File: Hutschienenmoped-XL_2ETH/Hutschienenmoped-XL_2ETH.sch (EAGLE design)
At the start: 118 parts, among them J1 638207222005, J13 638207222005, J15 638207222008, J2 645004114822, J3 61302211821, J4 61300421121, J6 61302211821, J7 638207222005, J8 638207222007, U1 ESP32-S3-DEVKITC-1-N8R2, U4 TLE9250VSJ

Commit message: gitflow-feature-stash: ETH
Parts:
- removed J3, J6: 61302211821, Wurth_Connectors_WR-PHD:6130XX11821_61302211821
- added ESP32-J1, ESP32-J3: 61302211821, Wurth_Connectors_WR-PHD:6130XX11821_61302211821
- added J10: 61300811821, Wurth_Connectors_WR-PHD:6130XX11821_61300811821
- added J11: 61300611821, Wurth_Connectors_WR-PHD:6130XX11821_61300611821
- added J12: 61300615721, Wurth_Connectors_WR-PHD:6130XX15721_61300615721
- added J14: 61300815721, Wurth_Connectors_WR-PHD:6130XX15721_61300815721
- added MP1, MP2, MP3, MP4: M3 x 2.5mm, Wurth_Assembly_WA-SMSI:WA-SMSI_9774XXX360_9774025360R
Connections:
- removed net IX00: U1.GPIO14
- removed net IX06: U1.GPIO15
- removed net MB_UART_RTS1: U1.GPIO10
- removed net MB_UART_RXD1: U1.GPIO8
- removed net MB_UART_RXD2: U1.GPIO11
- removed net QX06: U1.GPIO48
- removed net QX07: U1.GPIO38
- net +3V3: now also ESP32-J1.1, ESP32-J1.2
- net +5V: now also ESP32-J1.21
- net BOOT: now also ESP32-J3.14
- net CAN1_RXD: now also ESP32-J1.5
- net CAN1_TXD: now also ESP32-J1.4
- net CI1: now also ESP32-J1.19
- net CI2: now also ESP32-J1.18
- net CI3: now also ESP32-J1.15
- net CI4: now also ESP32-J1.13
- net CI5: now also ESP32-J1.11
- net CI6: now also ESP32-J1.10
- net CI7: now also ESP32-J1.7
- net CI8: now also ESP32-J1.6
- net ECU_GND: now also ESP32-J1.22, ESP32-J3.1, ESP32-J3.21, ESP32-J3.22
- net Q1C: now also ESP32-J3.18
- net Q2C: now also ESP32-J3.17
- net Q3C: now also ESP32-J3.9
- net Q4C: now also ESP32-J3.8
- net Q5C: now also ESP32-J3.7
- net Q6C: now also ESP32-J3.6
- net Q7C: now also ESP32-J3.4
- net Q8C: now also ESP32-J3.5
- net RESET: now also ESP32-J1.3

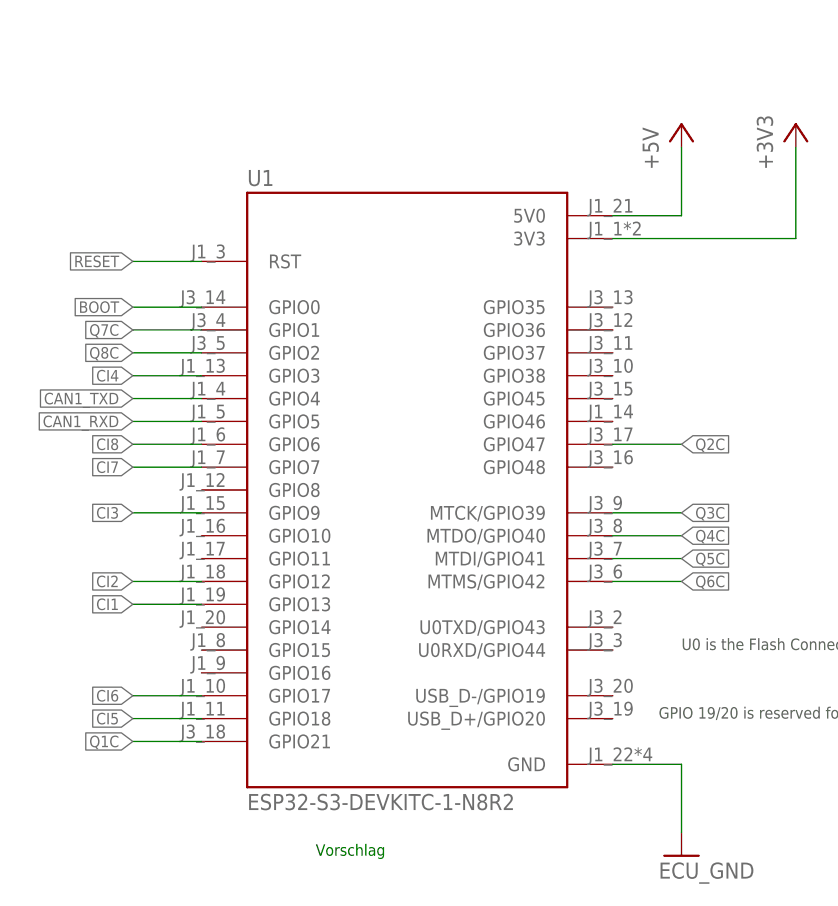
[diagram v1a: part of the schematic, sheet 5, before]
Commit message: Add new wire connections and curves in the board design.
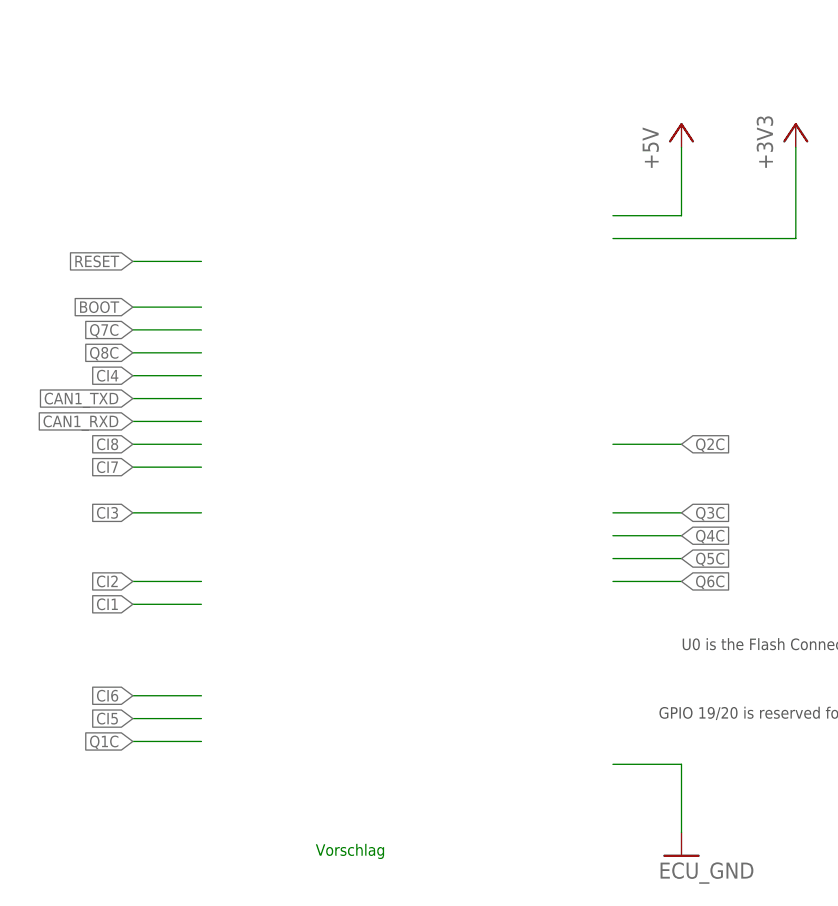
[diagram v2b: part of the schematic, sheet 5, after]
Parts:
- removed U1: ESP32-S3-DEVKITC-1-N8R2, ESP32-S3-DEVKITC-1-N8R2:ESP32-S3-DEVKITC-1-N8R2
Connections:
- net +3V3: no longer U1.3V3
- net +5V: no longer U1.5V0
- net BOOT: no longer U1.GPIO0
- net CAN1_RXD: no longer U1.GPIO5
- net CAN1_TXD: no longer U1.GPIO4
- net CI1: no longer U1.GPIO13
- net CI2: no longer U1.GPIO12
- net CI3: no longer U1.GPIO9
- net CI4: no longer U1.GPIO3
- net CI5: no longer U1.GPIO18
- net CI6: no longer U1.GPIO17
- net CI7: no longer U1.GPIO7
- net CI8: no longer U1.GPIO6
- net ECU_GND: no longer U1.GND
- net Q1C: no longer U1.GPIO21
- net Q2C: no longer U1.GPIO47
- net Q3C: no longer U1.MTCK/GPIO39
- net Q4C: no longer U1.MTDO/GPIO40
- net Q5C: no longer U1.MTDI/GPIO41
- net Q6C: no longer U1.MTMS/GPIO42
- net Q7C: no longer U1.GPIO1
- net Q8C: no longer U1.GPIO2
- net RESET: no longer U1.RST
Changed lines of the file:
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@@
 <part name="D3" library="Wurth_LEDs_WL-SMTW" library_urn="urn:adsk.eagle:library:19062651" deviceset="WL-SMTW_3528" device="" package3d_urn="urn:adsk.eagle:package:19062500/6" technology="_150141VS73100" value="150141VS73100"/>
 <part name="FRAME3" library="frames" library_urn="urn:adsk.eagle:library:229" deviceset="A4L-LOC" device=""/>
-<part name="U1" library="ESP32-S3-DEVKITC-1-N8R2" library_urn="urn:adsk.eagle:library:34329045" deviceset="ESP32-S3-DEVKITC-1-N8R2" device="" package3d_urn="urn:adsk.eagle:package:34329048/2"/>
 <part name="+3V4" library="supply1" library_urn="urn:adsk.eagle:library:371" deviceset="+3V3" device=""/>
 <part name="P+5" library="supply1" library_urn="urn:adsk.eagle:library:371" deviceset="+5V" device=""/>
@@
 <attribute name="SHEET" x="230.505" y="5.08" size="2.54" layer="94" font="vector"/>
 </instance>
-<instance part="U1" gate="G$1" x="111.76" y="83.82" smashed="yes">
-<attribute name="NAME" x="93.98" y="119.38" size="1.778" layer="95" align="top-left"/>
-<attribute name="VALUE" x="93.98" y="48.26" size="1.778" layer="96"/>
-</instance>
 <instance part="+3V4" gate="G$1" x="154.94" y="124.46" smashed="yes">
 <attribute name="VALUE" x="152.4" y="119.38" size="1.778" layer="96" rot="R90"/>
@@
 <net name="+3V3" class="0">
 <segment>
-<pinref part="U1" gate="G$1" pin="3V3"/>
 <pinref part="+3V4" gate="G$1" pin="+3V3"/>
 <wire x1="134.62" y1="111.76" x2="154.94" y2="111.76" width="0.1524" layer="91"/>
@@
 <net name="CAN1_TXD" class="0">
 <segment>
-<pinref part="U1" gate="G$1" pin="GPIO4"/>
 <wire x1="88.9" y1="93.98" x2="81.28" y2="93.98" width="0.1524" layer="91"/>
 <label x="81.28" y="93.98" size="1.27" layer="95" rot="R180" xref="yes"/>
@@
 <net name="CAN1_RXD" class="0">
 <segment>
-<pinref part="U1" gate="G$1" pin="GPIO5"/>
 <wire x1="88.9" y1="91.44" x2="81.28" y2="91.44" width="0.1524" layer="91"/>
 <label x="81.28" y="91.44" size="1.27" layer="95" rot="R180" xref="yes"/>
@@
 <net name="CI7" class="0">
 <segment>
-<pinref part="U1" gate="G$1" pin="GPIO7"/>
 <wire x1="88.9" y1="86.36" x2="81.28" y2="86.36" width="0.1524" layer="91"/>
 <label x="81.28" y="86.36" size="1.27" layer="95" rot="R180" xref="yes"/>
@@
 <net name="CI5" class="0">
 <segment>
-<pinref part="U1" gate="G$1" pin="GPIO18"/>
 <wire x1="88.9" y1="58.42" x2="81.28" y2="58.42" width="0.1524" layer="91"/>
 <label x="81.28" y="58.42" size="1.27" layer="95" rot="R180" xref="yes"/>
@@
 <net name="CI8" class="0">
 <segment>
-<pinref part="U1" gate="G$1" pin="GPIO6"/>
 <wire x1="88.9" y1="88.9" x2="81.28" y2="88.9" width="0.1524" layer="91"/>
 <label x="81.28" y="88.9" size="1.27" layer="95" rot="R180" xref="yes"/>
@@
 <net name="Q1C" class="0">
 <segment>
-<pinref part="U1" gate="G$1" pin="GPIO21"/>
 <wire x1="88.9" y1="55.88" x2="81.28" y2="55.88" width="0.1524" layer="91"/>
 <label x="81.28" y="55.88" size="1.27" layer="95" rot="R180" xref="yes"/>
@@
 <net name="Q3C" class="0">
 <segment>
-<pinref part="U1" gate="G$1" pin="MTCK/GPIO39"/>
 <wire x1="134.62" y1="81.28" x2="142.24" y2="81.28" width="0.1524" layer="91"/>
 <label x="142.24" y="81.28" size="1.27" layer="95" xref="yes"/>
@@
 <net name="BOOT" class="0">
 <segment>
-<pinref part="U1" gate="G$1" pin="GPIO0"/>
 <wire x1="88.9" y1="104.14" x2="81.28" y2="104.14" width="0.1524" layer="91"/>
 <label x="81.28" y="104.14" size="1.27" layer="95" rot="R180" xref="yes"/>
@@
 <net name="RESET" class="0">
 <segment>
-<pinref part="U1" gate="G$1" pin="RST"/>
 <wire x1="88.9" y1="109.22" x2="81.28" y2="109.22" width="0.1524" layer="91"/>
 <label x="81.28" y="109.22" size="1.27" layer="95" rot="R180" xref="yes"/>
@@
 <net name="CI4" class="0">
 <segment>
-<pinref part="U1" gate="G$1" pin="GPIO3"/>
 <wire x1="88.9" y1="96.52" x2="81.28" y2="96.52" width="0.1524" layer="91"/>
 <label x="81.28" y="96.52" size="1.27" layer="95" rot="R180" xref="yes"/>
@@
 <net name="CI6" class="0">
 <segment>
-<pinref part="U1" gate="G$1" pin="GPIO17"/>
 <wire x1="88.9" y1="60.96" x2="81.28" y2="60.96" width="0.1524" layer="91"/>
 <label x="81.28" y="60.96" size="1.27" layer="95" rot="R180" xref="yes"/>
@@
 <net name="Q5C" class="0">
 <segment>
-<pinref part="U1" gate="G$1" pin="MTDI/GPIO41"/>
 <wire x1="134.62" y1="76.2" x2="142.24" y2="76.2" width="0.1524" layer="91"/>
 <label x="142.24" y="76.2" size="1.27" layer="95" xref="yes"/>
@@
 <net name="Q4C" class="0">
 <segment>
-<pinref part="U1" gate="G$1" pin="MTDO/GPIO40"/>
 <wire x1="134.62" y1="78.74" x2="142.24" y2="78.74" width="0.1524" layer="91"/>
 <label x="142.24" y="78.74" size="1.27" layer="95" xref="yes"/>
@@
 <net name="Q6C" class="0">
 <segment>
-<pinref part="U1" gate="G$1" pin="MTMS/GPIO42"/>
 <wire x1="134.62" y1="73.66" x2="142.24" y2="73.66" width="0.1524" layer="91"/>
 <label x="142.24" y="73.66" size="1.27" layer="95" xref="yes"/>
@@
 <net name="Q8C" class="0">
 <segment>
-<pinref part="U1" gate="G$1" pin="GPIO2"/>
 <wire x1="88.9" y1="99.06" x2="81.28" y2="99.06" width="0.1524" layer="91"/>
 <label x="81.28" y="99.06" size="1.27" layer="95" rot="R180" xref="yes"/>
@@
 <net name="Q2C" class="0">
 <segment>
-<pinref part="U1" gate="G$1" pin="GPIO47"/>
 <wire x1="134.62" y1="88.9" x2="142.24" y2="88.9" width="0.1524" layer="91"/>
 <label x="142.24" y="88.9" size="1.27" layer="95" xref="yes"/>
@@
 <net name="CI3" class="0">
 <segment>
-<pinref part="U1" gate="G$1" pin="GPIO9"/>
 <wire x1="88.9" y1="81.28" x2="81.28" y2="81.28" width="0.1524" layer="91"/>
 <label x="81.28" y="81.28" size="1.27" layer="95" rot="R180" xref="yes"/>
@@
 <net name="CI2" class="0">
 <segment>
-<pinref part="U1" gate="G$1" pin="GPIO12"/>
 <wire x1="88.9" y1="73.66" x2="81.28" y2="73.66" width="0.1524" layer="91"/>
 <label x="81.28" y="73.66" size="1.27" layer="95" rot="R180" xref="yes"/>
@@
 <net name="CI1" class="0">
 <segment>
-<pinref part="U1" gate="G$1" pin="GPIO13"/>
 <wire x1="88.9" y1="71.12" x2="81.28" y2="71.12" width="0.1524" layer="91"/>
 <label x="81.28" y="71.12" size="1.27" layer="95" rot="R180" xref="yes"/>
@@
 <net name="Q7C" class="0">
 <segment>
-<pinref part="U1" gate="G$1" pin="GPIO1"/>
 <wire x1="88.9" y1="101.6" x2="81.28" y2="101.6" width="0.1524" layer="91"/>
 <label x="81.28" y="101.6" size="1.27" layer="95" rot="R180" xref="yes"/>
@@
 <net name="ECU_GND" class="1">
 <segment>
-<pinref part="U1" gate="G$1" pin="GND"/>
 <wire x1="134.62" y1="53.34" x2="142.24" y2="53.34" width="0.1524" layer="91"/>
 <wire x1="142.24" y1="53.34" x2="142.24" y2="45.72" width="0.1524" layer="91"/>
@@
 <net name="+5V" class="0">
 <segment>
-<pinref part="U1" gate="G$1" pin="5V0"/>
 <pinref part="P+5" gate="1" pin="+5V"/>
 <wire x1="134.62" y1="114.3" x2="142.24" y2="114.3" width="0.1524" layer="91"/>

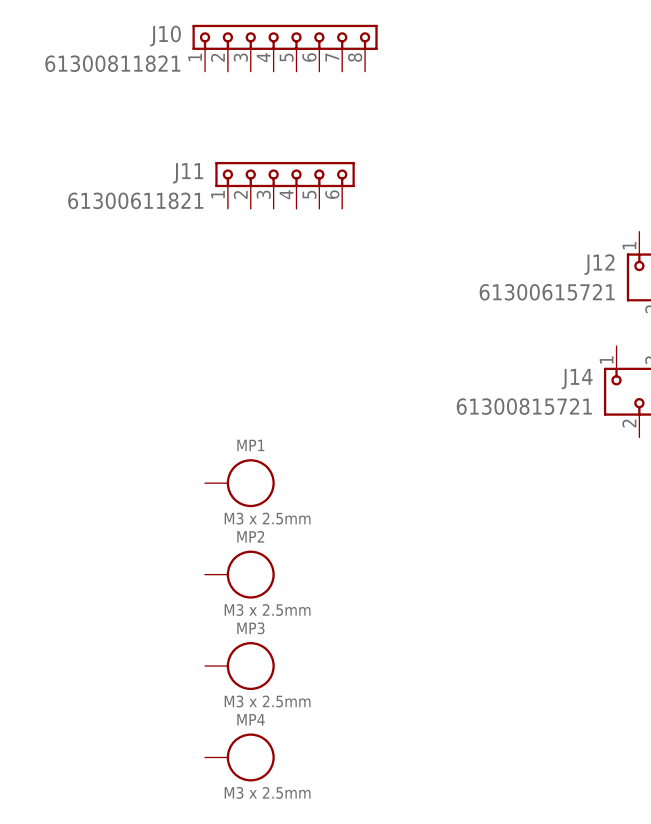
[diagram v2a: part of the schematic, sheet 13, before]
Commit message: Update grid settings to display grid lines, add wires for a new component. Remove redundant package elements and attributes.
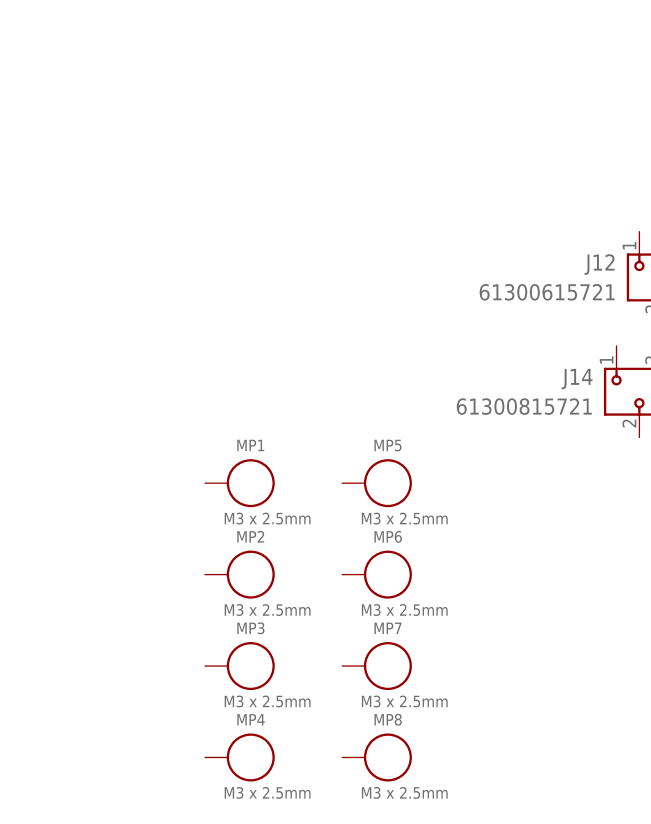
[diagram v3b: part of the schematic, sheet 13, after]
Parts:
- removed J10: 61300811821, Wurth_Connectors_WR-PHD:6130XX11821_61300811821
- removed J11: 61300611821, Wurth_Connectors_WR-PHD:6130XX11821_61300611821
- added MP5, MP6, MP7, MP8: M3 x 2.5mm, Wurth_Assembly_WA-SMSI:WA-SMSI_9774XXX360_9774025360R
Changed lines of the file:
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@@
 <part name="J1" library="Wurth_Connectors_WR-FAST" library_urn="urn:adsk.eagle:library:15267884" deviceset="638207222005" device="" package3d_urn="urn:adsk.eagle:package:15267960/3" value=" 638207222005 "/>
 <part name="J2" library="Wurth_Connectors_WR-WTB" library_urn="urn:adsk.eagle:library:15818693" deviceset="645004114822" device="" package3d_urn="urn:adsk.eagle:package:15819025/2" value="645004114822"/>
-<part name="J10" library="Wurth_Connectors_WR-PHD" library_urn="urn:adsk.eagle:library:14804658" deviceset="6130XX11821_61300811821" device="" package3d_urn="urn:adsk.eagle:package:14805545/3" value=" 61300811821 "/>
-<part name="J11" library="Wurth_Connectors_WR-PHD" library_urn="urn:adsk.eagle:library:14804658" deviceset="6130XX11821_61300611821" device="" package3d_urn="urn:adsk.eagle:package:14805543/3" value=" 61300611821 "/>
 <part name="MP1" library="Wurth_Assembly_WA-SMSI" library_urn="urn:adsk.eagle:library:14418591" deviceset="WA-SMSI_9774XXX360" device="_9774025360R" package3d_urn="urn:adsk.eagle:package:14321862/4" value="M3 x 2.5mm"/>
 <part name="MP2" library="Wurth_Assembly_WA-SMSI" library_urn="urn:adsk.eagle:library:14418591" deviceset="WA-SMSI_9774XXX360" device="_9774025360R" package3d_urn="urn:adsk.eagle:package:14321862/4" value="M3 x 2.5mm"/>
@@
 <part name="FRAME1" library="frames" library_urn="urn:adsk.eagle:library:229" deviceset="A4L-LOC" device=""/>
 <part name="P+1" library="supply1" library_urn="urn:adsk.eagle:library:371" deviceset="+5V" device=""/>
+<part name="MP5" library="Wurth_Assembly_WA-SMSI" library_urn="urn:adsk.eagle:library:14418591" deviceset="WA-SMSI_9774XXX360" device="_9774025360R" package3d_urn="urn:adsk.eagle:package:14321862/4" value="M3 x 2.5mm"/>
+<part name="MP6" library="Wurth_Assembly_WA-SMSI" library_urn="urn:adsk.eagle:library:14418591" deviceset="WA-SMSI_9774XXX360" device="_9774025360R" package3d_urn="urn:adsk.eagle:package:14321862/4" value="M3 x 2.5mm"/>
+<part name="MP7" library="Wurth_Assembly_WA-SMSI" library_urn="urn:adsk.eagle:library:14418591" deviceset="WA-SMSI_9774XXX360" device="_9774025360R" package3d_urn="urn:adsk.eagle:package:14321862/4" value="M3 x 2.5mm"/>
+<part name="MP8" library="Wurth_Assembly_WA-SMSI" library_urn="urn:adsk.eagle:library:14418591" deviceset="WA-SMSI_9774XXX360" device="_9774025360R" package3d_urn="urn:adsk.eagle:package:14321862/4" value="M3 x 2.5mm"/>
 </parts>
 <sheets>
@@
 </plain>
 <instances>
-<instance part="J10" gate="G$1" x="68.58" y="170.18" smashed="yes">
-<attribute name="NAME" x="58.42" y="168.402" size="1.778" layer="95" align="bottom-right"/>
-<attribute name="VALUE" x="58.42" y="165.1" size="1.778" layer="96" align="bottom-right"/>
-</instance>
-<instance part="J11" gate="G$1" x="71.12" y="154.94" smashed="yes">
-<attribute name="NAME" x="60.96" y="153.162" size="1.778" layer="95" align="bottom-right"/>
-<attribute name="VALUE" x="60.96" y="149.86" size="1.778" layer="96" align="bottom-right"/>
-</instance>
 <instance part="MP1" gate="G$1" x="66.04" y="119.38" smashed="yes">
 <attribute name="NAME" x="66.04" y="122.936" size="1.27" layer="95" align="bottom-center"/>
@@
 <attribute name="VALUE" x="104.14" y="127" size="1.778" layer="96" align="bottom-right"/>
 </instance>
+<instance part="MP5" gate="G$1" x="81.28" y="119.38" smashed="yes">
+<attribute name="NAME" x="81.28" y="122.936" size="1.27" layer="95" align="bottom-center"/>
+<attribute name="VALUE" x="78.232" y="114.808" size="1.27" layer="95"/>
+</instance>
+<instance part="MP6" gate="G$1" x="81.28" y="109.22" smashed="yes">
+<attribute name="NAME" x="81.28" y="112.776" size="1.27" layer="95" align="bottom-center"/>
+<attribute name="VALUE" x="78.232" y="104.648" size="1.27" layer="95"/>
+</instance>
+<instance part="MP7" gate="G$1" x="81.28" y="99.06" smashed="yes">
+<attribute name="NAME" x="81.28" y="102.616" size="1.27" layer="95" align="bottom-center"/>
+<attribute name="VALUE" x="78.232" y="94.488" size="1.27" layer="95"/>
+</instance>
+<instance part="MP8" gate="G$1" x="81.28" y="88.9" smashed="yes">
+<attribute name="NAME" x="81.28" y="92.456" size="1.27" layer="95" align="bottom-center"/>
+<attribute name="VALUE" x="78.232" y="84.328" size="1.27" layer="95"/>
+</instance>
 </instances>
